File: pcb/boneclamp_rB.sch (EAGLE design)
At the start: 70 parts, among them IC1 24C, U1 AD8032ARZ-REEL7, U2 LT1964ES5-5TRMPBF, U4 TLV70245DBVT, U7 AD7682BCPZ, U8 TPS63700DRCT, U9 ADA4841-2YRZ

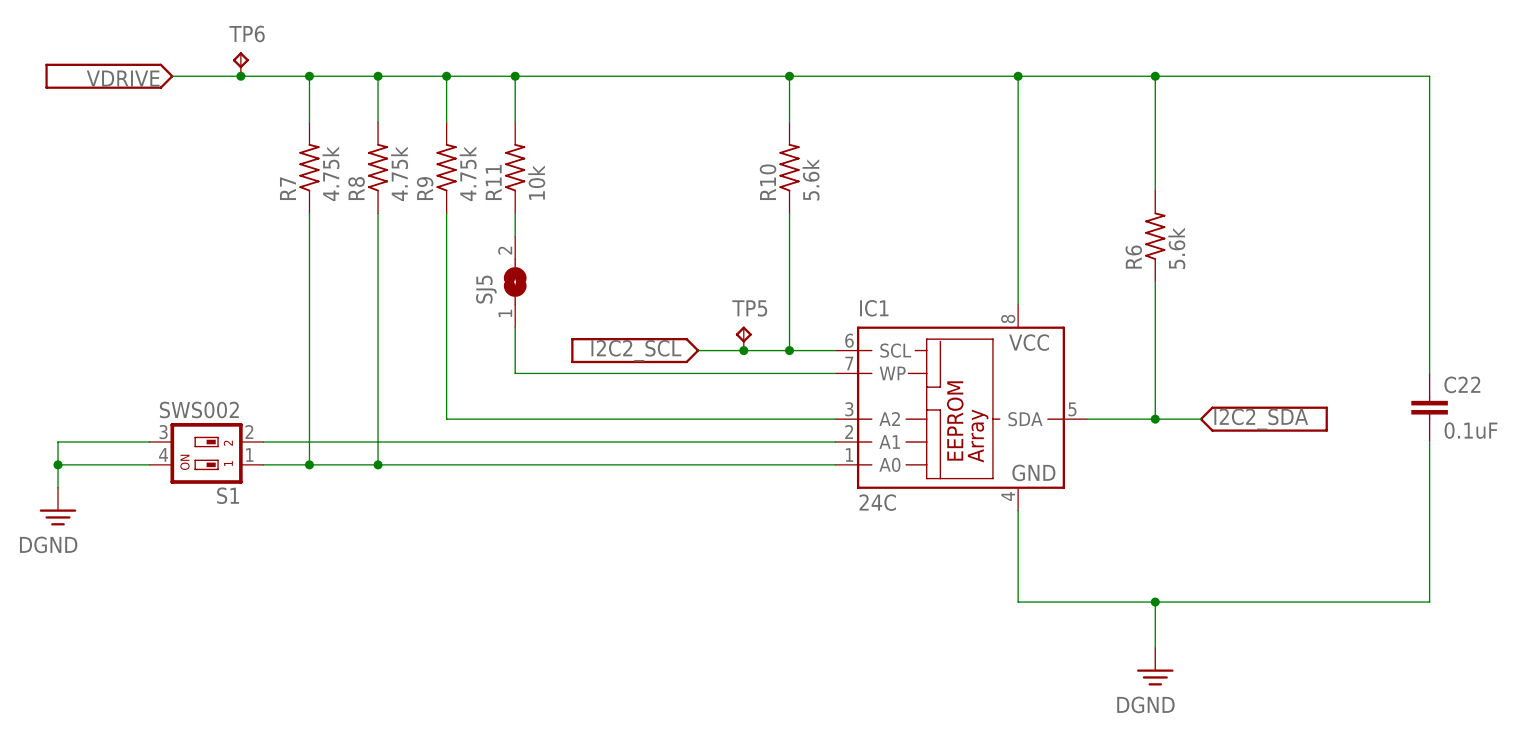
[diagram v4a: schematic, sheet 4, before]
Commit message: Minor fixed to EEPROM circuit and ADC VREF buffer. Stephano, don't kill me.
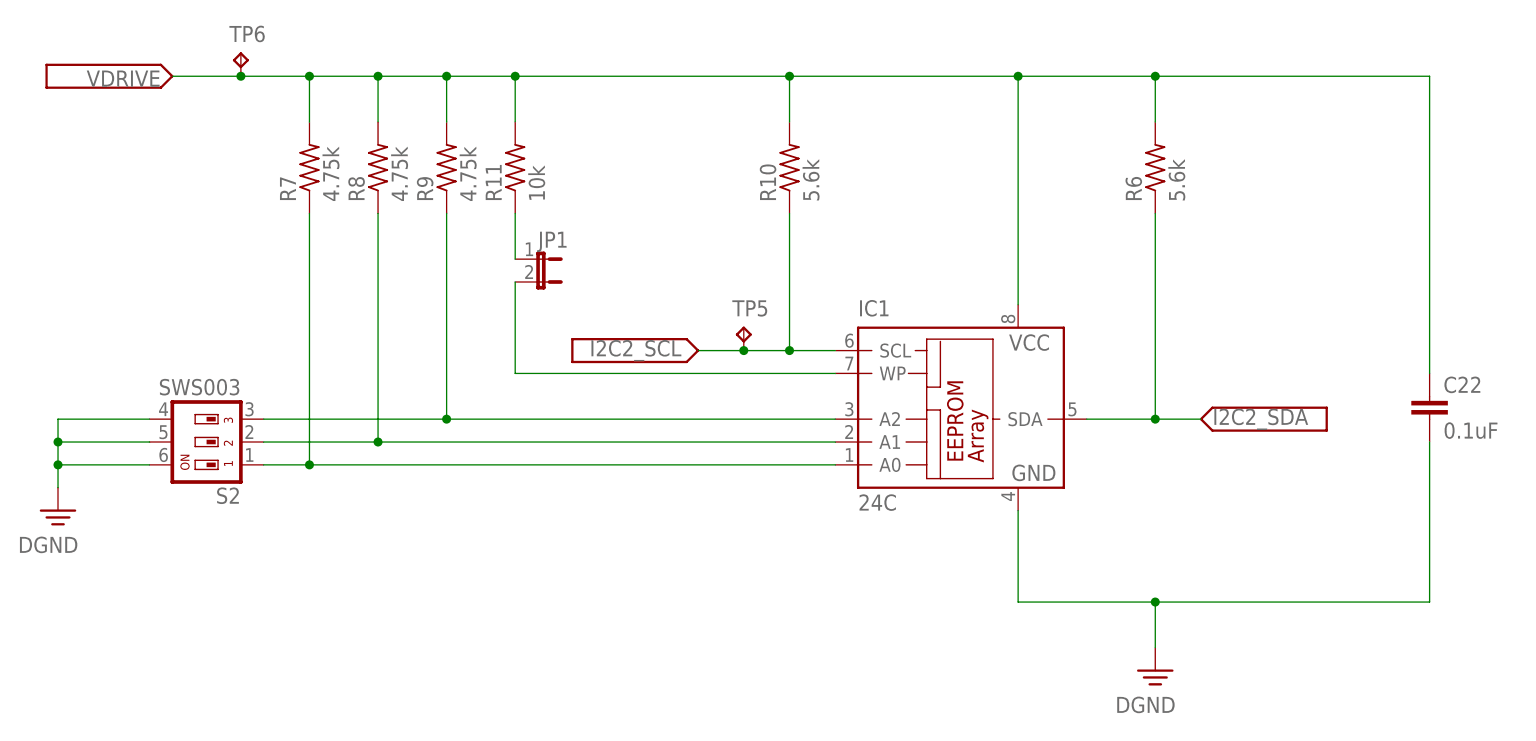
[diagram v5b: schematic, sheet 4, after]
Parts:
- removed S1: SWS002, smd-special:SWS002
- removed SJ5: (no value), jumper:SJ
- added C2: 0.1uF, rcl:C-EUC0805
- added JP1: (no value), jumper:JP1E
- added S2: SWS003, smd-special:SWS003
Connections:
- net N$12 renamed ADC_CNV
- net AGND: now also C2.2
- net DGND: now also S2.4, S2.5, S2.6; no longer S1.3, S1.4
- net N$14: now also S2.1; no longer R8.1, S1.1
- net N$18: now also R8.1, S2.2; no longer S1.2
- net N$19: now also S2.3
- net N$21: now also JP1.2; no longer SJ5.1
- net N$22: now also JP1.1; no longer SJ5.2
- net VDD: now also C2.1
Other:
- moved on the sheet: R6
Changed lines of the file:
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@@
 <part name="U$36" library="boneclamp" deviceset="V_SIG" device=""/>
 <part name="U$38" library="boneclamp" deviceset="V_SIG" device=""/>
-<part name="S1" library="smd-special" deviceset="SWS002" device=""/>
 <part name="C22" library="rcl" deviceset="C-EU" device="C0603" value="0.1uF"/>
 <part name="U$39" library="boneclamp" deviceset="V_SIG" device=""/>
@@
 <part name="R10" library="rcl" deviceset="R-US_" device="R0603" value="5.6k"/>
 <part name="R11" library="rcl" deviceset="R-US_" device="R0603" value="10k"/>
-<part name="SJ5" library="jumper" deviceset="SJ" device=""/>
 <part name="U$41" library="boneclamp" deviceset="V_SIG" device=""/>
 <part name="U$42" library="analog-devices-02" deviceset="AD5686RARUZ" device="" value="AD5686"/>
@@
 <part name="U$58" library="boneclamp" deviceset="V_SIG" device=""/>
 <part name="U$59" library="boneclamp" deviceset="V_SIG" device=""/>
+<part name="JP1" library="jumper" deviceset="JP1E" device=""/>
+<part name="S2" library="smd-special" deviceset="SWS003" device=""/>
+<part name="C2" library="rcl" deviceset="C-EU" device="C0805" value="0.1uF"/>
+<part name="SUPPLY4" library="supply2" deviceset="AGND" device=""/>
 </parts>
 <sheets>
@@
 <instance part="R14" gate="G$1" x="63.5" y="10.16" rot="R180"/>
 <instance part="C10" gate="G$1" x="73.66" y="-22.86"/>
-<instance part="U$9" gate="G$1" x="91.44" y="33.02" rot="R180"/>
+<instance part="U$9" gate="G$1" x="73.66" y="33.02" rot="R180"/>
 <instance part="U$11" gate="G$1" x="165.1" y="15.24"/>
 <instance part="C11" gate="G$1" x="50.8" y="-22.86"/>
@@
 <instance part="SJ8" gate="1" x="-55.88" y="7.62"/>
 <instance part="ADC_SDID" gate="G$1" x="-63.5" y="7.62" rot="MR0"/>
+<instance part="C2" gate="G$1" x="81.28" y="25.4"/>
+<instance part="SUPPLY4" gate="G$1" x="81.28" y="15.24"/>
 </instances>
 <busses>
@@
 <junction x="104.14" y="-53.34"/>
 </segment>
+<segment>
+<pinref part="C2" gate="G$1" pin="2"/>
+<wire x1="81.28" y1="20.32" x2="81.28" y2="17.78" width="0.1524" layer="91"/>
+<pinref part="SUPPLY4" gate="G$1" pin="AGND"/>
+</segment>
 </net>
 <net name="VDD" class="0">
 <segment>
 <wire x1="116.84" y1="15.24" x2="96.52" y2="15.24" width="0.1524" layer="91"/>
-<label x="90.17" y="34.29" size="1.778" layer="95" rot="R180"/>
+<label x="72.39" y="34.29" size="1.778" layer="95" rot="R180"/>
 <pinref part="U1" gate="A" pin="+VS"/>
 <wire x1="96.52" y1="15.24" x2="96.52" y2="33.02" width="0.1524" layer="91"/>
-<wire x1="96.52" y1="33.02" x2="91.44" y2="33.02" width="0.1524" layer="91"/>
+<wire x1="96.52" y1="33.02" x2="81.28" y2="33.02" width="0.1524" layer="91"/>
+<pinref part="C2" gate="G$1" pin="1"/>
+<wire x1="81.28" y1="33.02" x2="73.66" y2="33.02" width="0.1524" layer="91"/>
+<wire x1="81.28" y1="27.94" x2="81.28" y2="33.02" width="0.1524" layer="91"/>
+<junction x="81.28" y="33.02"/>
 </segment>
 <segment>
@@
 </segment>
 </net>
-<net name="N$12" class="0">
+<net name="ADC_CNV" class="0">
 <segment>
 <pinref part="U7" gate="A" pin="CNV"/>
 <wire x1="-33.02" y1="17.78" x2="-17.78" y2="17.78" width="0.1524" layer="91"/>
+<label x="-46.355" y="17.145" size="1.778" layer="95"/>
 </segment>
 </net>
@@
 <instances>
 <instance part="IC1" gate="G$1" x="-2.54" y="22.86"/>
-<instance part="S1" gate="G$1" x="-83.82" y="17.78" rot="R90"/>
 <instance part="C22" gate="G$1" x="50.8" y="25.4"/>
 <instance part="U$39" gate="G$1" x="-88.9" y="60.96" rot="R180"/>
 <instance part="DGND4" gate="PE" x="20.32" y="-5.08"/>
-<instance part="R6" gate="G$1" x="20.32" y="43.18" rot="R90"/>
+<instance part="R6" gate="G$1" x="20.32" y="50.8" rot="R90"/>
 <instance part="U$40" gate="G$1" x="25.4" y="22.86"/>
 <instance part="DGND8" gate="PE" x="-101.6" y="12.7"/>
@@
 <instance part="R10" gate="G$1" x="-20.32" y="50.8" rot="R90"/>
 <instance part="R11" gate="G$1" x="-50.8" y="50.8" rot="R90"/>
-<instance part="SJ5" gate="1" x="-50.8" y="38.1" rot="R90"/>
 <instance part="U$41" gate="G$1" x="-30.48" y="30.48" rot="R180"/>
 <instance part="TP5" gate="G$1" x="-25.4" y="33.02"/>
 <instance part="TP6" gate="G$1" x="-81.28" y="63.5"/>
+<instance part="JP1" gate="A" x="-48.26" y="40.64" rot="R270"/>
+<instance part="S2" gate="G$1" x="-83.82" y="20.32" rot="R90"/>
 </instances>
 <busses>
@@
 <wire x1="50.8" y1="60.96" x2="50.8" y2="27.94" width="0.1524" layer="91"/>
 <pinref part="R6" gate="G$1" pin="2"/>
-<wire x1="20.32" y1="48.26" x2="20.32" y2="60.96" width="0.1524" layer="91"/>
+<wire x1="20.32" y1="55.88" x2="20.32" y2="60.96" width="0.1524" layer="91"/>
 <junction x="20.32" y="60.96"/>
 <pinref part="R7" gate="G$1" pin="2"/>
@@
 </segment>
 <segment>
-<pinref part="S1" gate="G$1" pin="3"/>
 <wire x1="-91.44" y1="20.32" x2="-101.6" y2="20.32" width="0.1524" layer="91"/>
 <wire x1="-101.6" y1="20.32" x2="-101.6" y2="17.78" width="0.1524" layer="91"/>
-<pinref part="S1" gate="G$1" pin="4"/>
 <wire x1="-101.6" y1="17.78" x2="-91.44" y2="17.78" width="0.1524" layer="91"/>
 <wire x1="-101.6" y1="17.78" x2="-101.6" y2="15.24" width="0.1524" layer="91"/>
 <junction x="-101.6" y="17.78"/>
 <pinref part="DGND8" gate="PE" pin="PE"/>
+<pinref part="S2" gate="G$1" pin="5"/>
+<pinref part="S2" gate="G$1" pin="6"/>
+<wire x1="-101.6" y1="20.32" x2="-101.6" y2="22.86" width="0.1524" layer="91"/>
+<junction x="-101.6" y="20.32"/>
+<pinref part="S2" gate="G$1" pin="4"/>
+<wire x1="-101.6" y1="22.86" x2="-91.44" y2="22.86" width="0.1524" layer="91"/>
 </segment>
 </net>
@@
 <pinref part="IC1" gate="G$1" pin="SDA"/>
 <wire x1="12.7" y1="22.86" x2="20.32" y2="22.86" width="0.1524" layer="91"/>
-<wire x1="20.32" y1="38.1" x2="20.32" y2="22.86" width="0.1524" layer="91"/>
+<wire x1="20.32" y1="45.72" x2="20.32" y2="22.86" width="0.1524" layer="91"/>
 <pinref part="R6" gate="G$1" pin="1"/>
 <wire x1="20.32" y1="22.86" x2="25.4" y2="22.86" width="0.1524" layer="91"/>
@@
 <net name="N$14" class="0">
 <segment>
-<pinref part="S1" gate="G$1" pin="1"/>
 <pinref part="IC1" gate="G$1" pin="A0"/>
 <wire x1="-78.74" y1="17.78" x2="-73.66" y2="17.78" width="0.1524" layer="91"/>
-<wire x1="-73.66" y1="17.78" x2="-66.04" y2="17.78" width="0.1524" layer="91"/>
-<wire x1="-66.04" y1="17.78" x2="-15.24" y2="17.78" width="0.1524" layer="91"/>
-<wire x1="-66.04" y1="17.78" x2="-66.04" y2="45.72" width="0.1524" layer="91"/>
-<junction x="-66.04" y="17.78"/>
+<wire x1="-73.66" y1="17.78" x2="-15.24" y2="17.78" width="0.1524" layer="91"/>
 <wire x1="-73.66" y1="17.78" x2="-73.66" y2="45.72" width="0.1524" layer="91"/>
 <junction x="-73.66" y="17.78"/>
 <pinref part="R7" gate="G$1" pin="1"/>
+<pinref part="S2" gate="G$1" pin="1"/>
+</segment>
+</net>
+<net name="N$18" class="0">
+<segment>
+<pinref part="IC1" gate="G$1" pin="A1"/>
+<wire x1="-15.24" y1="20.32" x2="-66.04" y2="20.32" width="0.1524" layer="91"/>
+<pinref part="S2" gate="G$1" pin="2"/>
 <pinref part="R8" gate="G$1" pin="1"/>
-</segment>
-</net>
-<net name="N$18" class="0">
-<segment>
-<pinref part="IC1" gate="G$1" pin="A1"/>
-<pinref part="S1" gate="G$1" pin="2"/>
-<wire x1="-15.24" y1="20.32" x2="-78.74" y2="20.32" width="0.1524" layer="91"/>
+<wire x1="-66.04" y1="20.32" x2="-78.74" y2="20.32" width="0.1524" layer="91"/>
+<wire x1="-66.04" y1="45.72" x2="-66.04" y2="20.32" width="0.1524" layer="91"/>
+<junction x="-66.04" y="20.32"/>
 </segment>
 </net>
@@
 <wire x1="-58.42" y1="22.86" x2="-58.42" y2="45.72" width="0.1524" layer="91"/>
 <pinref part="R9" gate="G$1" pin="1"/>
+<pinref part="S2" gate="G$1" pin="3"/>
+<wire x1="-78.74" y1="22.86" x2="-58.42" y2="22.86" width="0.1524" layer="91"/>
+<junction x="-58.42" y="22.86"/>
 </segment>
 </net>
@@
 <segment>
 <pinref part="R11" gate="G$1" pin="1"/>
-<pinref part="SJ5" gate="1" pin="2"/>
-<wire x1="-50.8" y1="45.72" x2="-50.8" y2="43.18" width="0.1524" layer="91"/>
+<pinref part="JP1" gate="A" pin="1"/>
+<wire x1="-50.8" y1="40.64" x2="-50.8" y2="45.72" width="0.1524" layer="91"/>
 </segment>
 </net>
 <net name="N$21" class="0">
 <segment>
-<pinref part="SJ5" gate="1" pin="1"/>
-<wire x1="-50.8" y1="33.02" x2="-50.8" y2="27.94" width="0.1524" layer="91"/>
 <pinref part="IC1" gate="G$1" pin="WP"/>
 <wire x1="-50.8" y1="27.94" x2="-15.24" y2="27.94" width="0.1524" layer="91"/>
-</segment>
-</net>
+<pinref part="JP1" gate="A" pin="2"/>
+<wire x1="-50.8" y1="27.94" x2="-50.8" y2="38.1" width="0.1524" layer="91"/>
+</segment>
+</net>

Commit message: Minor edit
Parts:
- added TP7: TPB1,27, testpad:TPB1,27
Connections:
- net I2C2_SDA: now also TP7.TP
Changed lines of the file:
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@@
 <setting verticaltext="up"/>
 </settings>
-<grid distance="0.025" unitdist="inch" unit="inch" style="lines" multiple="1" display="no" altdistance="0.01" altunitdist="inch" altunit="inch"/>
+<grid distance="0.1" unitdist="inch" unit="inch" style="lines" multiple="1" display="no" altdistance="0.01" altunitdist="inch" altunit="inch"/>
 <layers>
 <layer number="1" name="Top" color="4" fill="1" visible="no" active="no"/>
@@
 <part name="C2" library="rcl" deviceset="C-EU" device="C0805" value="0.1uF"/>
 <part name="SUPPLY4" library="supply2" deviceset="AGND" device=""/>
+<part name="TP7" library="testpad" deviceset="TP" device="B1,27"/>
 </parts>
 <sheets>
@@
 <instance part="JP1" gate="A" x="-48.26" y="40.64" rot="R270"/>
 <instance part="S2" gate="G$1" x="-83.82" y="20.32" rot="R90"/>
+<instance part="TP7" gate="G$1" x="15.24" y="25.4"/>
 </instances>
 <busses>
@@
 <segment>
 <pinref part="IC1" gate="G$1" pin="SDA"/>
-<wire x1="12.7" y1="22.86" x2="20.32" y2="22.86" width="0.1524" layer="91"/>
+<wire x1="12.7" y1="22.86" x2="15.24" y2="22.86" width="0.1524" layer="91"/>
+<wire x1="15.24" y1="22.86" x2="20.32" y2="22.86" width="0.1524" layer="91"/>
 <wire x1="20.32" y1="45.72" x2="20.32" y2="22.86" width="0.1524" layer="91"/>
 <pinref part="R6" gate="G$1" pin="1"/>
@@
 <junction x="20.32" y="22.86"/>
 <label x="26.67" y="22.225" size="1.778" layer="95"/>
-</segment>
-</net>
+<pinref part="TP7" gate="G$1" pin="TP"/>
+<junction x="15.24" y="22.86"/>
+</segment>
+</net>

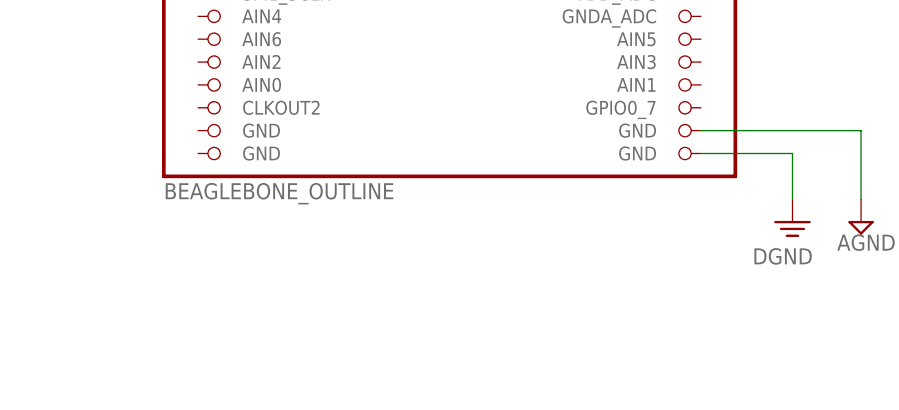
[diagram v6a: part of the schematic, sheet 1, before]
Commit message: Added p6 to the schematic of the BB, update the BC shematic and board
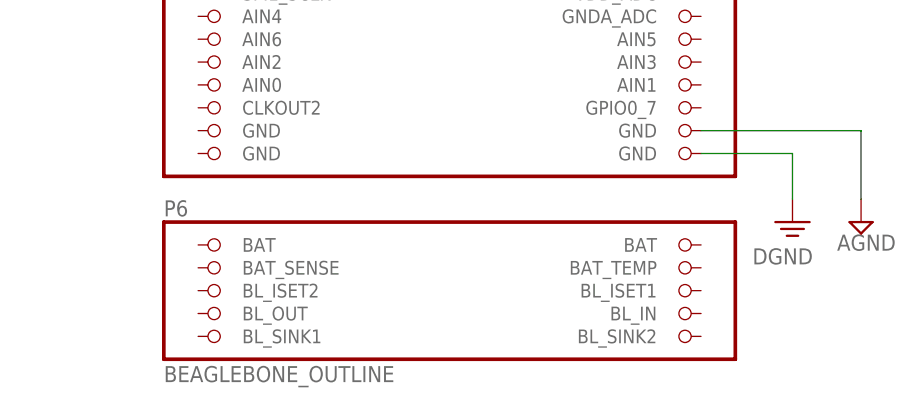
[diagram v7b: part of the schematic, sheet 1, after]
